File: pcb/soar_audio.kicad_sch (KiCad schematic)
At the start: 107 parts, among them J1 RJ45-FLAPS, J2 RJ12-FLAPS, J3 HEADER_4, J4 Screw_Terminal_01x02, J5 RJ45-CAN, J6 HEADER_4, J7 HEADER_2, J8 HEADER_4, J9 HEADER_4, Q1 AO3401A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

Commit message: some minor changes
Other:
- title: (none) -> the SOAR Utility
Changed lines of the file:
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@@
 (kicad_sch (version 20211123) (generator eeschema)
   (paper "A3")
+  (title_block
+    (title "the SOAR Utility")
+    (date "2022-01-05")
+    (rev "v1.0")
+  )
   (junction (at 196.85 234.95) (diameter 0) (color 0 0 0 0)
   )

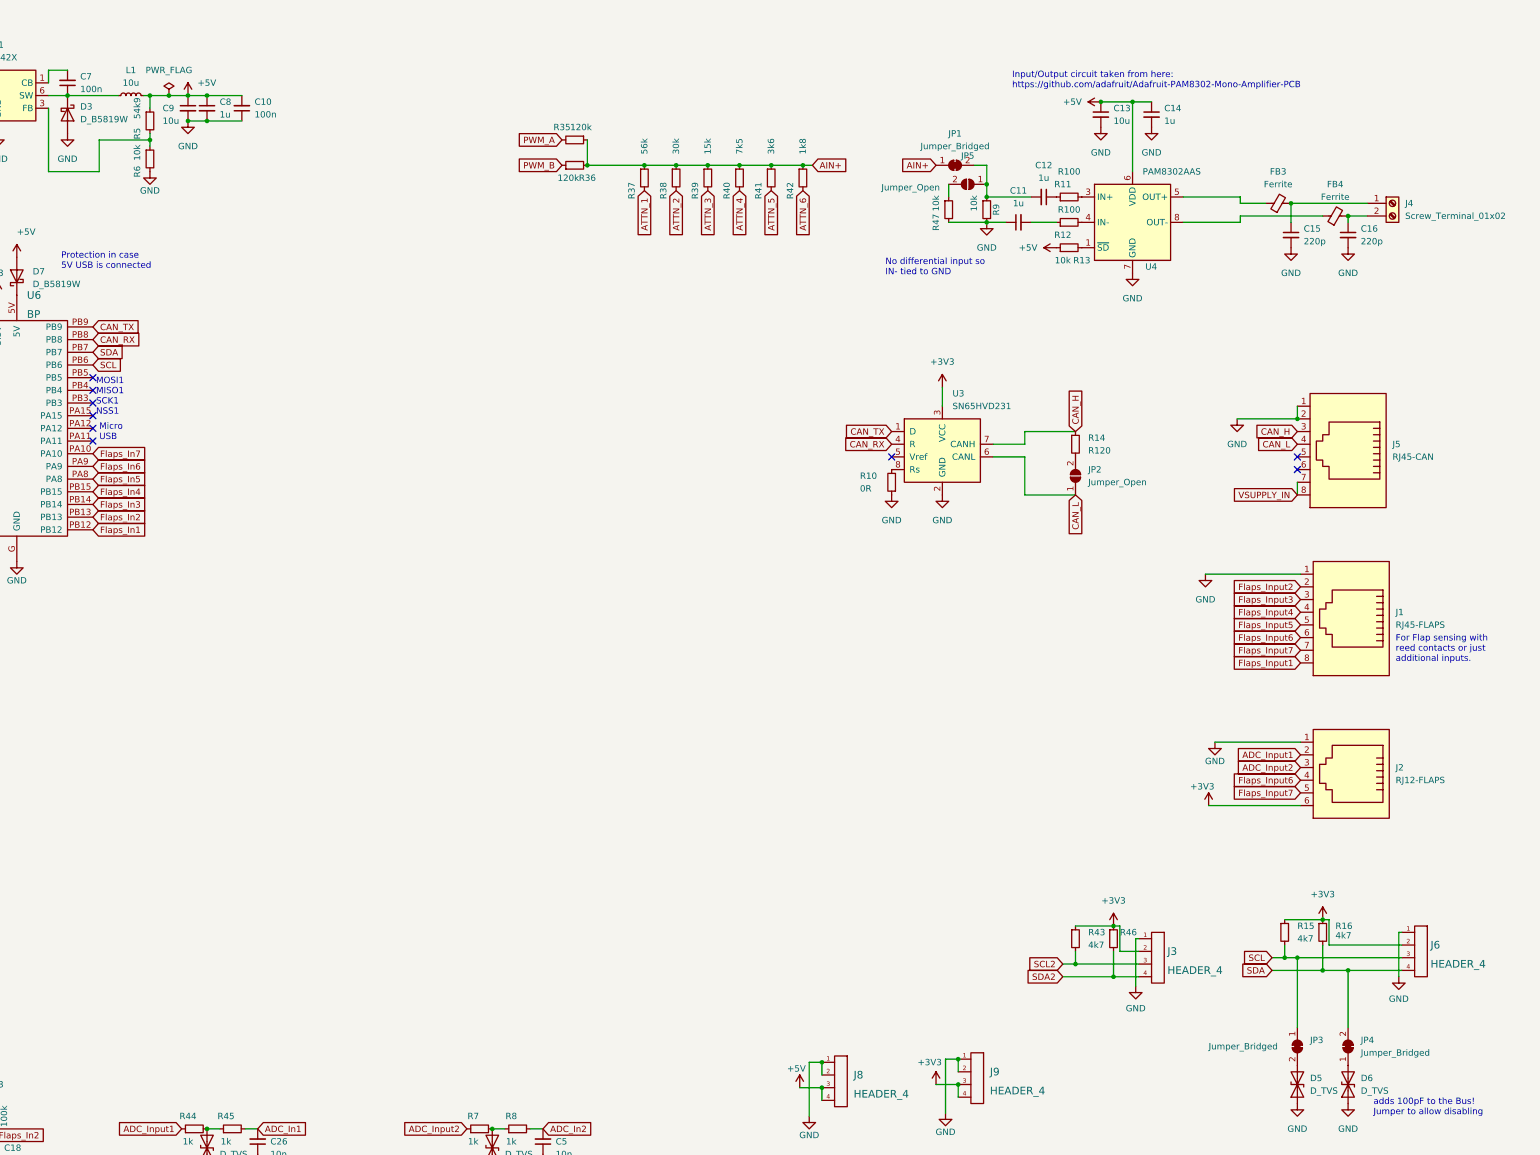
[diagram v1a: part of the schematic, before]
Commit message: updates based on feedback from Klaus
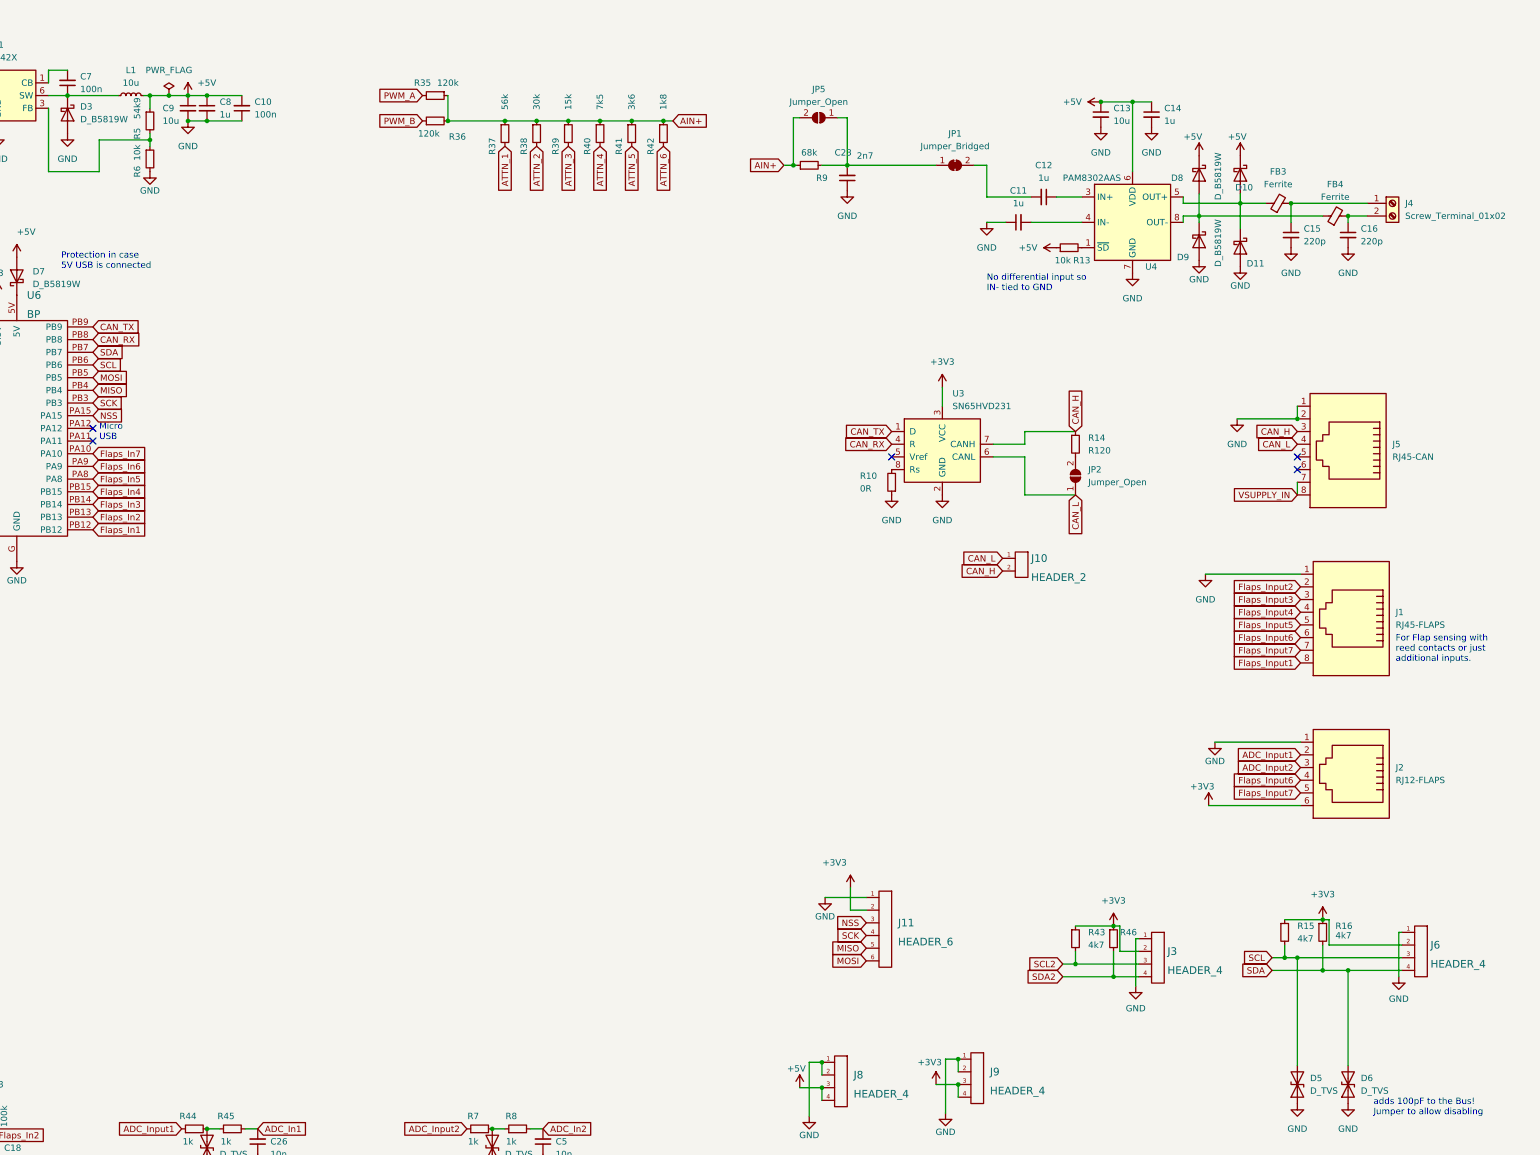
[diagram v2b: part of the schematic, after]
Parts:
- removed JP3, JP4: Jumper_Bridged, Jumper:SolderJumper-2_P1.3mm_Bridged_Pad1.0x1.5mm, symbol Jumper:SolderJumper_2_Bridged
- removed R11, R12: R100, Resistor_SMD:R_0603_1608Metric, symbol Device:R_Small
- removed R47: 10k, Resistor_SMD:R_0603_1608Metric, symbol Device:R_Small
- added C23: 2n7, Capacitor_SMD:C_0603_1608Metric, symbol Device:C_Small
- added D10, D11, D8, D9: D_B5819W, Diode_SMD:D_SOD-123, symbol Device:D_Schottky
- added J10: HEADER_2, Connector_PinHeader_1.27mm:PinHeader_1x02_P1.27mm_Vertical, symbol STM32F4Di:HEADER_2
- added J11: HEADER_6, Connector_PinHeader_1.27mm:PinHeader_1x06_P1.27mm_Vertical, symbol STM32F4Di:HEADER_6
- R9: value 10k -> 68k; LCSC C25804 -> C23231
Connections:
- net +3V3: now also J11.2
- net +5V: now also D10.1 (K), D8.1 (K)
- net AIN+: now also JP5.2 (B), R9.1; no longer JP1.1 (A)
- net CAN_H: now also J10.2
- net CAN_L: now also J10.1
- net GND: now also C23.1, D11.2 (A), D9.2 (A), J11.1; no longer R9.2
- net SCL: now also D5.2 (A2)
- net SDA: now also D6.2 (A2)
- net NSS: now reaches U6.PA15
- net NSS: now also J11.3
- net SCK: now reaches U6.PB3
- net SCK: now also J11.4
- net MISO: now reaches U6.PB4
- net MISO: now also J11.5
- net MOSI: now reaches U6.PB5
- net MOSI: now also J11.6
- net at C12.2, JP1.2 (B): no longer JP5.1 (A), R9.1
- net at C11.2: now also U4.4 (IN-)
- net at C12.1: now also U4.3 (IN+)
- net at FB3.1, U4.5 (OUT+): now also D10.2 (A), D11.1 (K)
- net at FB4.1, U4.8 (OUT-): now also D8.2 (A), D9.1 (K)
- new net: C23.2, JP1.1 (A), JP5.1 (A), R9.2
- no-connect marks 15 -> 11
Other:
- note removed: "Input/Output circuit taken from here: https://github.com/adafruit/Adafruit-PAM8302-Mono-Amplifier-PCB"
- note removed: "MOSI1 MISO1 SCK1 NSS1"
- moved on the sheet: R35, R36, R37, R38, R39, R40, R41, R42

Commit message: finalized pcb and generated v1.0 production files
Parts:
- removed R43, R46: 4k7, Resistor_SMD:R_0603_1608Metric, symbol Device:R_Small
- added C24, C25, C27, C28, C29: 100n, Capacitor_SMD:C_0603_1608Metric, symbol Device:C_Small
- added U2: MAX3232, Package_SO:HTSSOP-16-1EP_4.4x5mm_P0.65mm_EP3x3mm, symbol Interface_UART:MAX3232
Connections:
- net +3V3: now also C25.2, U2.16 (VCC)
- net GND: now also C25.1, C28.1, C29.1, U2.15 (GND)
- net SCL2 renamed RS232_RX
- net RS232_RX: now also U2.13 (R1IN); no longer U6.PB10
- net SDA2 renamed RS232_TX
- net RS232_TX: now also U2.14 (T1OUT); no longer U6.PB11
- new net: C29.2, U2.6 (VS-)
- new net: C27.1, U2.5 (C2-)
- new net: C27.2, U2.4 (C2+)
- new net: C24.2, U2.1 (C1+)
- new net: C28.2, U2.2 (VS+)
- new net: C24.1, U2.3 (C1-)
- new net UART_RX: U2.12 (R1OUT), U6.PB11
- new net UART_TX: U2.11 (T1IN), U6.PB10
- no-connect marks 11 -> 15
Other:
- moved on the sheet: J1, J10, J11, J2, J3, J8, J9

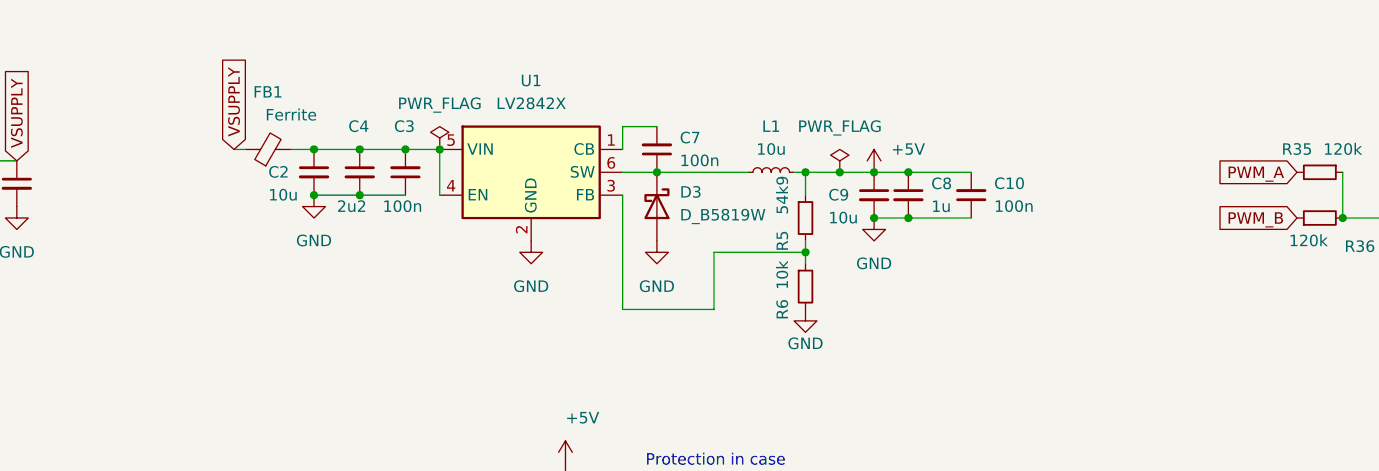
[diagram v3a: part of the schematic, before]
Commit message: changed dc-dc converter
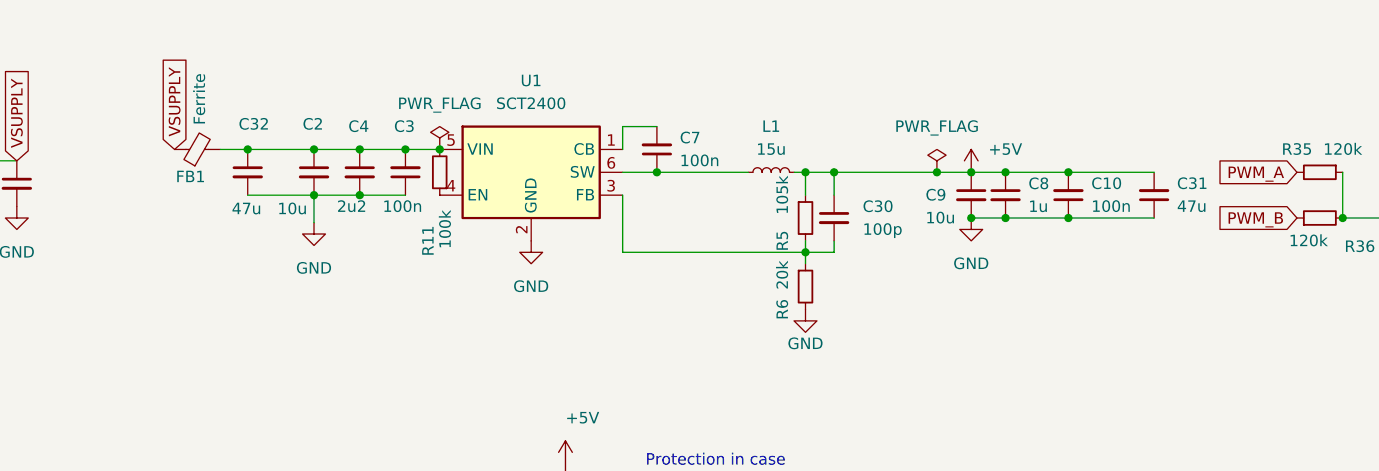
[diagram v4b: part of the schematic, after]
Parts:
- removed D3: D_B5819W, Diode_SMD:D_SOD-123, symbol Device:D_Schottky
- added C30: 100p, Capacitor_SMD:C_0603_1608Metric, symbol Device:C_Small
- added C31, C32: 47u, Capacitor_SMD:C_1206_3216Metric, symbol Device:C_Small
- added R11: 100k, Resistor_SMD:R_0603_1608Metric, symbol Device:R_Small
- L1: value 10u -> 15u; footprint OWN_PARTS:MWSA0402S -> OWN_PARTS:SLO0630H; LCSC C408339 -> C182182
- R5: value 54k9 -> 105k; LCSC C23077 -> C16840
- R6: value 10k -> 20k; LCSC C25804 -> C4184
- U1: value LV2842X -> SCT2400; LCSC C225807 -> C2693819
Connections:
- net +5V: now also C30.1, C31.2
- net GND: now also C31.1, C32.2
- net at C2.1, C3.2, C4.1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: now also C32.1, R11.2; no longer U1.4 (EN)
- net at R5.2, R6.1, U1.3 (FB): now also C30.2
- new net: R11.1, U1.4 (EN)
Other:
- moved on the sheet: C10, C8, C9, FB1
